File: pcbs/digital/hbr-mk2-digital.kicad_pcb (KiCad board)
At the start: 2 copper layers, 59 x 93 mm, 97 parts, among them J1 Conn_01x09, J10 Conn_01x06, J11 Conn_01x05, J12 Conn_01x02, J13 Conn_01x02, J14 Conn_01x02, J2 Conn_01x02, J3 Conn_01x04, J4 Conn_01x04, J5 Conn_01x03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

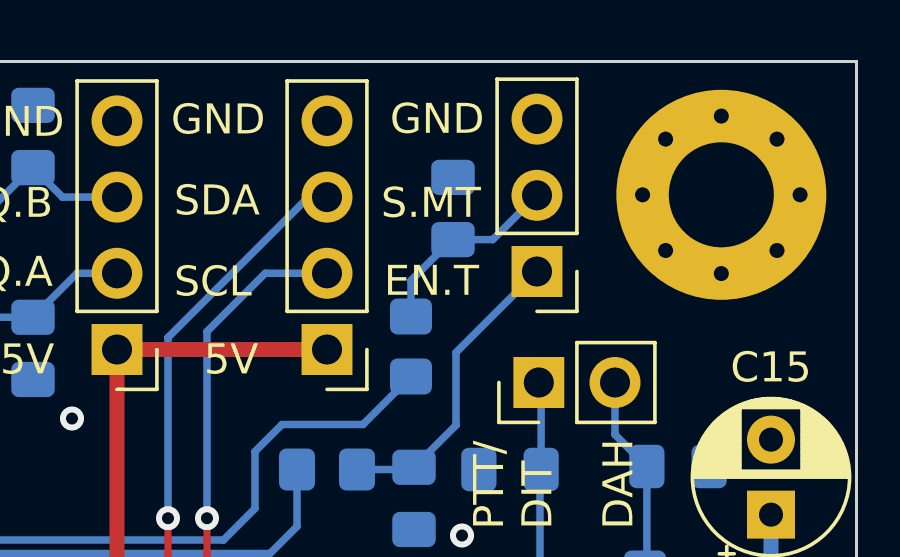
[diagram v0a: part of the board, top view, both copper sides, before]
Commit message: Digital board: correct the silkscreen
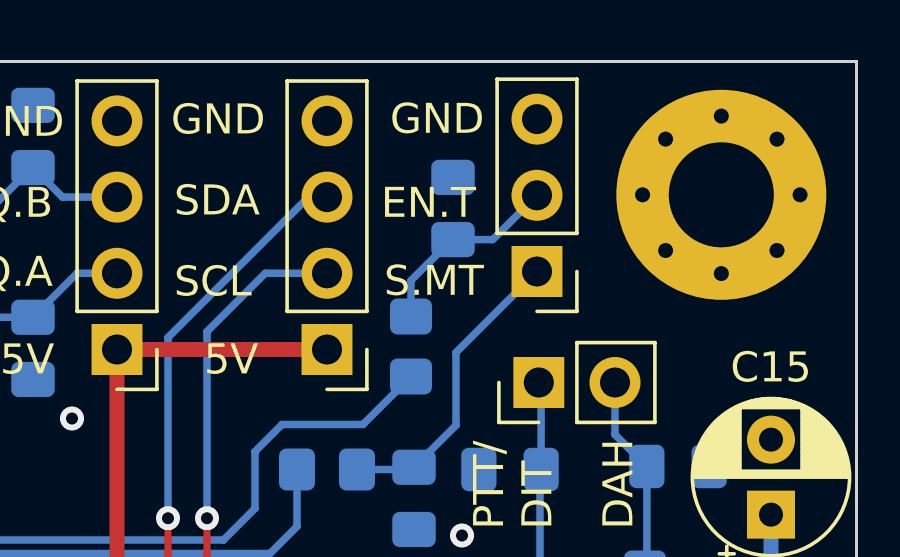
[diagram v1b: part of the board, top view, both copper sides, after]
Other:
- board text added: "HBR/MK2 Digital Board v1.1 Aleksander Alekseev R2AUK, 2024 https://github.com/afiskon/hbr-mk2"
- board text removed: "HBR/MK2 Digital Board v1.0 Aleksander Alekseev R2AUK, 2024 https://github.com/afiskon/hbr-mk2"
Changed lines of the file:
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@@
   (gr_line (start 175.75 138) (end 116.75 138)
     (stroke (width 0.1) (type default)) (layer "Edge.Cuts"))
-  (gr_text "HBR/MK2 Digital Board v1.0\nAleksander Alekseev R2AUK, 2024\nhttps://github.com/afiskon/hbr-mk2" (at 132.8 79.9 90) (layer "B.SilkS")
+  (gr_text "HBR/MK2 Digital Board v1.1\nAleksander Alekseev R2AUK, 2024\nhttps://github.com/afiskon/hbr-mk2" (at 132.8 79.9 90) (layer "B.SilkS")
     (effects (font (size 1 1) (thickness 0.15)) (justify left bottom mirror))
   )
@@
     (effects (font (size 1 1) (thickness 0.15)) (justify left bottom))
   )
-  (gr_text "EN.T" (at 160 52.9) (layer "F.SilkS")
+  (gr_text "S.MT" (at 160 52.9) (layer "F.SilkS")
     (effects (font (size 1 1) (thickness 0.15)) (justify left bottom))
   )
@@
     (effects (font (size 1 1) (thickness 0.15)) (justify left bottom))
   )
-  (gr_text "S.MT" (at 159.9 50.3) (layer "F.SilkS")
+  (gr_text "EN.T" (at 159.9 50.3) (layer "F.SilkS")
     (effects (font (size 1 1) (thickness 0.15)) (justify left bottom))
   )
